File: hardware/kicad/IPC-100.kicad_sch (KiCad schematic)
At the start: 0 parts

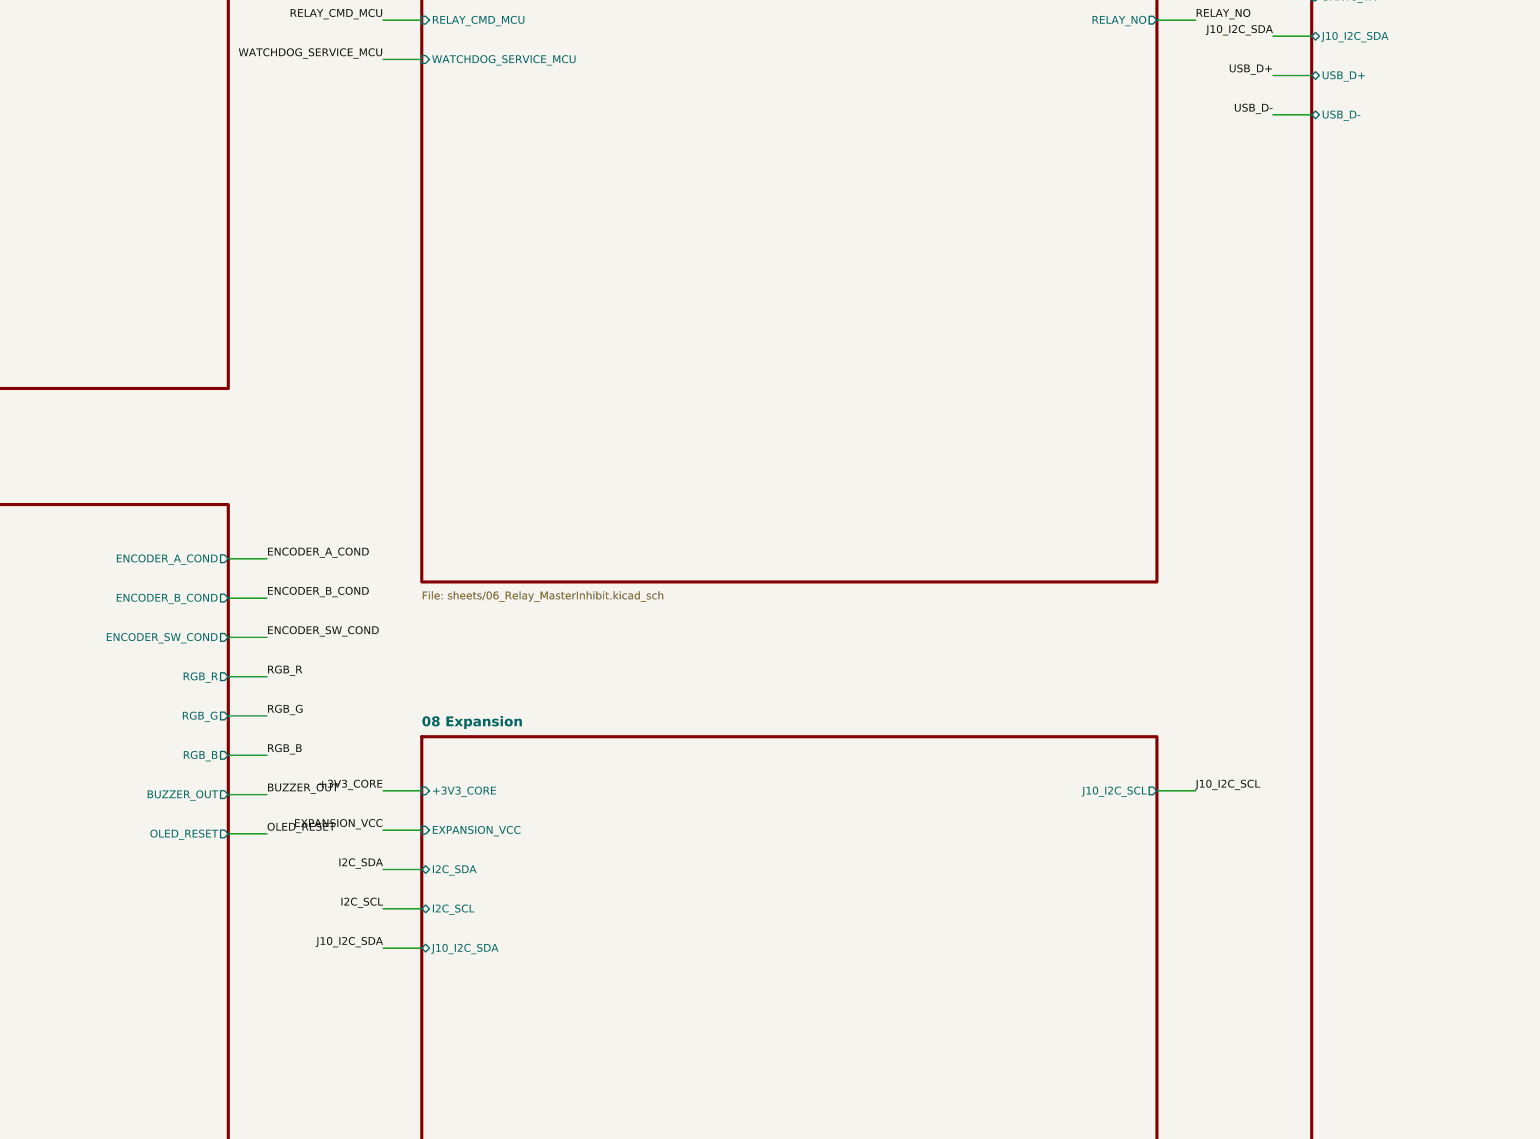
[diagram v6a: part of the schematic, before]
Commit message: Complete ECO-003 hierarchy exposure
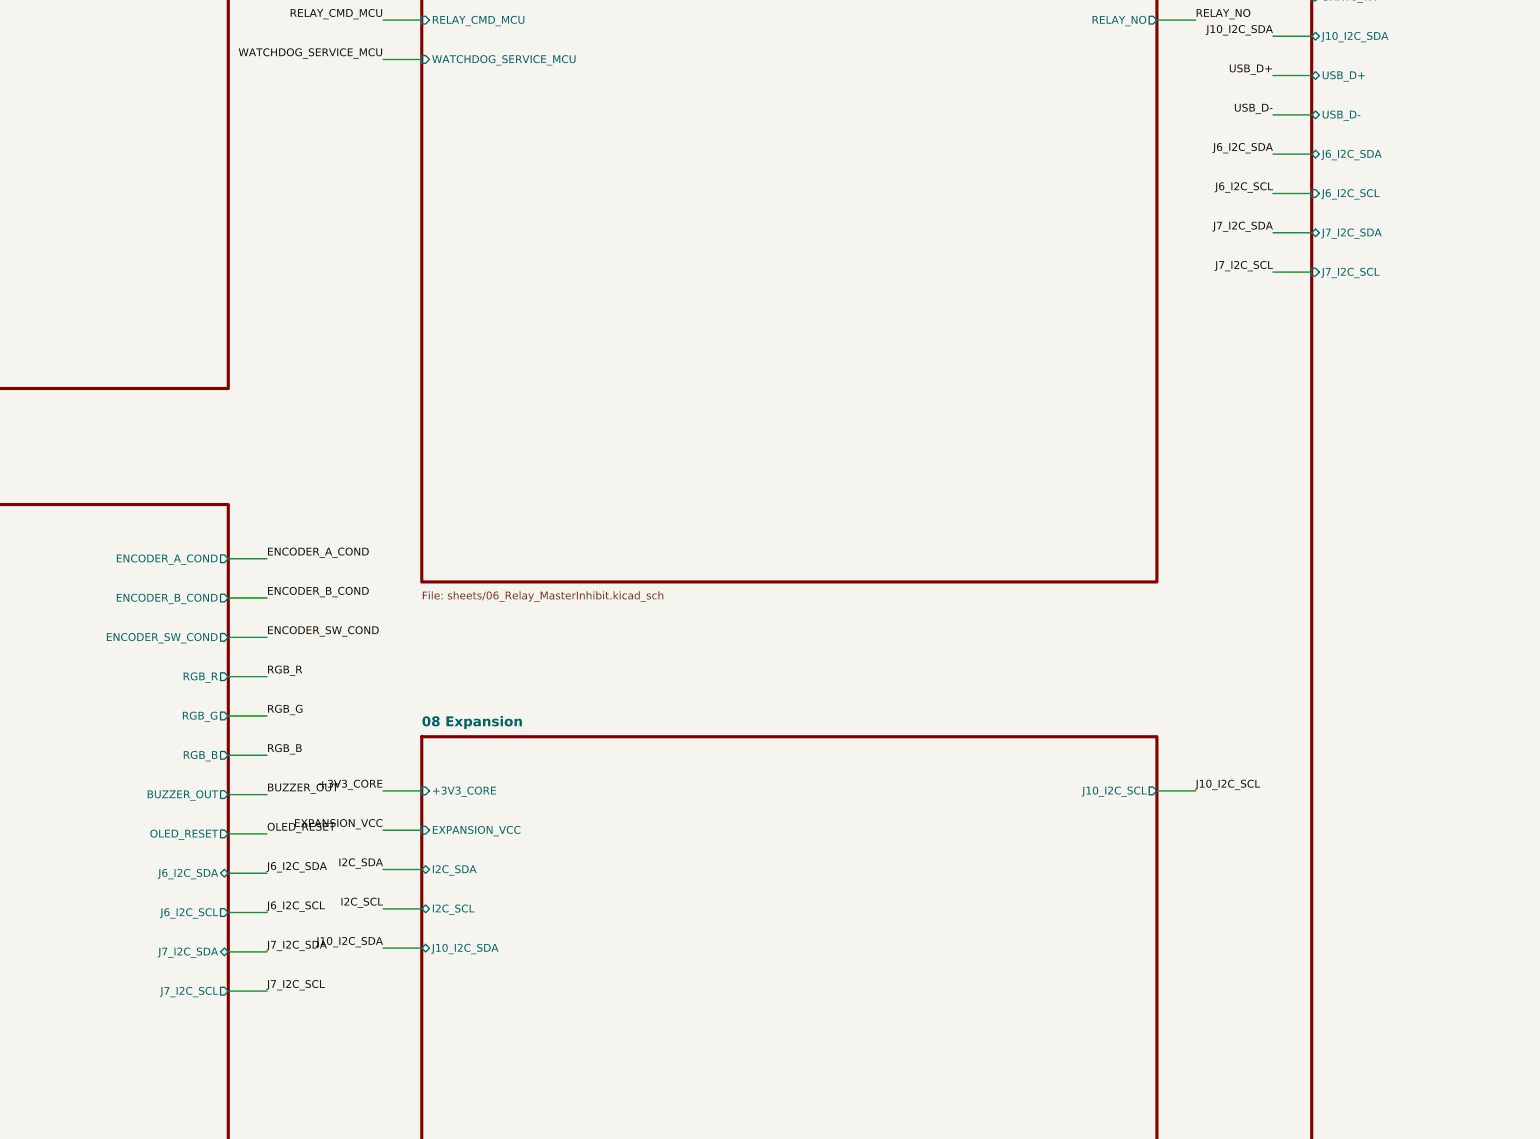
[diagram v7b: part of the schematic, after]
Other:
- sheet 07 UI + OLED + Sensor ports: added J6_I2C_SCL, J6_I2C_SDA, J7_I2C_SCL, J7_I2C_SDA; removed none
- sheet 09 Connectors + Test Access ports: added J6_I2C_SCL, J6_I2C_SDA, J7_I2C_SCL, J7_I2C_SDA; removed none
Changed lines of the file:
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@@
+      (effects (font (size 1.0 1.0)) (justify right))
+    )
+    (pin "J6_I2C_SDA" bidirectional (at 350 337.64 0)
+      (effects (font (size 1.0 1.0)) (justify right))
+    )
+    (pin "J6_I2C_SCL" output (at 350 342.72 0)
+      (effects (font (size 1.0 1.0)) (justify right))
+    )
+    (pin "J7_I2C_SDA" bidirectional (at 350 347.80 0)
+      (effects (font (size 1.0 1.0)) (justify right))
+    )
+    (pin "J7_I2C_SCL" output (at 350 352.88 0)
       (effects (font (size 1.0 1.0)) (justify right))
     )
@@
   )
   (label "OLED_RESET" (at 355 332.56 0)
+    (effects (font (size 1.0 1.0)) (justify left bottom))
+  )
+  (wire (pts (xy 350 337.64) (xy 355 337.64))
+    (stroke (width 0) (type default))
+  )
+  (label "J6_I2C_SDA" (at 355 337.64 0)
+    (effects (font (size 1.0 1.0)) (justify left bottom))
+  )
+  (wire (pts (xy 350 342.72) (xy 355 342.72))
+    (stroke (width 0) (type default))
+  )
+  (label "J6_I2C_SCL" (at 355 342.72 0)
+    (effects (font (size 1.0 1.0)) (justify left bottom))
+  )
+  (wire (pts (xy 350 347.80) (xy 355 347.80))
+    (stroke (width 0) (type default))
+  )
+  (label "J7_I2C_SDA" (at 355 347.80 0)
+    (effects (font (size 1.0 1.0)) (justify left bottom))
+  )
+  (wire (pts (xy 350 352.88) (xy 355 352.88))
+    (stroke (width 0) (type default))
+  )
+  (label "J7_I2C_SCL" (at 355 352.88 0)
     (effects (font (size 1.0 1.0)) (justify left bottom))
   )
@@
       (effects (font (size 1.0 1.0)) (justify left))
     )
+    (pin "J6_I2C_SDA" bidirectional (at 490 244.72 180)
+      (effects (font (size 1.0 1.0)) (justify left))
+    )
+    (pin "J6_I2C_SCL" input (at 490 249.80 180)
+      (effects (font (size 1.0 1.0)) (justify left))
+    )
+    (pin "J7_I2C_SDA" bidirectional (at 490 254.88 180)
+      (effects (font (size 1.0 1.0)) (justify left))
+    )
+    (pin "J7_I2C_SCL" input (at 490 259.96 180)
+      (effects (font (size 1.0 1.0)) (justify left))
+    )
     (pin "VIN_RAW" output (at 580 72.00 0)
       (effects (font (size 1.0 1.0)) (justify right))
@@
     (effects (font (size 1.0 1.0)) (justify right bottom))
   )
+  (wire (pts (xy 490 244.72) (xy 485 244.72))
+    (stroke (width 0) (type default))
+  )
+  (label "J6_I2C_SDA" (at 485 244.72 180)
+    (effects (font (size 1.0 1.0)) (justify right bottom))
+  )
+  (wire (pts (xy 490 249.80) (xy 485 249.80))
+    (stroke (width 0) (type default))
+  )
+  (label "J6_I2C_SCL" (at 485 249.80 180)
+    (effects (font (size 1.0 1.0)) (justify right bottom))
+  )
+  (wire (pts (xy 490 254.88) (xy 485 254.88))
+    (stroke (width 0) (type default))
+  )
+  (label "J7_I2C_SDA" (at 485 254.88 180)
+    (effects (font (size 1.0 1.0)) (justify right bottom))
+  )
+  (wire (pts (xy 490 259.96) (xy 485 259.96))
+    (stroke (width 0) (type default))
+  )
+  (label "J7_I2C_SCL" (at 485 259.96 180)
+    (effects (font (size 1.0 1.0)) (justify right bottom))
+  )
